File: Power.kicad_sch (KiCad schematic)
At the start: 21 parts, among them IC1 TLV74033PDBVR, J4 USB_C_Receptacle_USB2.0_16P, J9 Conn_01x02, Q1 AO3401A, U3 CH340N, U4 CN3063, U5 TPS7A0522PDBV

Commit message: completed layout and routing with preliminary matching network
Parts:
- renumbered C19 to C20, C27 to C21, C20 to C22, C28 to C23, C30 to C24, C21 to C25, J4 to J2, J9 to J3, R7 to R5, R8 to R6, R5 to R7, R6 to R8, U4 to U3, IC1 to U4, U3 to U5, U5 to U6
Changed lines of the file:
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@@
 		(dnp no)
 		(fields_autoplaced yes)
-		(property "Reference" "#PWR017"
+		(property "Reference" "#PWR024"
 			(at 156.21 67.31 0)
 			(hide yes)
@@
 			(project "WINLAB-LP-Radio-Sensor-Hub"
 				(path "/0de7ee4a-bb98-4bc6-bb89-3afafc4b94b5/5ad374ff-424f-46b2-9f18-b4cecbd24790"
-					(reference "#PWR017")
+					(reference "#PWR024")
 					(unit 1)
 				)
@@
 		(dnp no)
 		(fields_autoplaced yes)
-		(property "Reference" "R7"
+		(property "Reference" "R5"
 			(at 78.74 121.9199 0)
 			(show_name no)
@@
 			(project "WINLAB-LP-Radio-Sensor-Hub"
 				(path "/0de7ee4a-bb98-4bc6-bb89-3afafc4b94b5/5ad374ff-424f-46b2-9f18-b4cecbd24790"
-					(reference "R7")
+					(reference "R5")
 					(unit 1)
 				)
@@
 		(dnp no)
 		(fields_autoplaced yes)
-		(property "Reference" "C20"
+		(property "Reference" "C22"
 			(at 153.67 78.7399 0)
 			(show_name no)
@@
 			(project "WINLAB-LP-Radio-Sensor-Hub"
 				(path "/0de7ee4a-bb98-4bc6-bb89-3afafc4b94b5/5ad374ff-424f-46b2-9f18-b4cecbd24790"
-					(reference "C20")
+					(reference "C22")
 					(unit 1)
 				)
@@
 		(dnp no)
 		(fields_autoplaced yes)
-		(property "Reference" "#PWR029"
+		(property "Reference" "#PWR019"
 			(at 68.58 115.57 0)
 			(hide yes)
@@
 			(project "WINLAB-LP-Radio-Sensor-Hub"
 				(path "/0de7ee4a-bb98-4bc6-bb89-3afafc4b94b5/5ad374ff-424f-46b2-9f18-b4cecbd24790"
-					(reference "#PWR029")
+					(reference "#PWR019")
 					(unit 1)
 				)
@@
 		(dnp no)
 		(fields_autoplaced yes)
-		(property "Reference" "C28"
+		(property "Reference" "C23"
 			(at 173.99 118.1099 0)
 			(show_name no)
@@
 			(project "WINLAB-LP-Radio-Sensor-Hub"
 				(path "/0de7ee4a-bb98-4bc6-bb89-3afafc4b94b5/5ad374ff-424f-46b2-9f18-b4cecbd24790"
-					(reference "C28")
+					(reference "C23")
 					(unit 1)
 				)
@@
 		(dnp no)
 		(fields_autoplaced yes)
-		(property "Reference" "IC1"
+		(property "Reference" "U4"
 			(at 153.67 105.41 0)
 			(show_name no)
@@
 			(project "WINLAB-LP-Radio-Sensor-Hub"
 				(path "/0de7ee4a-bb98-4bc6-bb89-3afafc4b94b5/5ad374ff-424f-46b2-9f18-b4cecbd24790"
-					(reference "IC1")
+					(reference "U4")
 					(unit 1)
 				)
@@
 		(dnp no)
 		(fields_autoplaced yes)
-		(property "Reference" "#PWR015"
+		(property "Reference" "#PWR021"
 			(at 92.71 67.31 0)
 			(hide yes)
@@
 			(project "WINLAB-LP-Radio-Sensor-Hub"
 				(path "/0de7ee4a-bb98-4bc6-bb89-3afafc4b94b5/5ad374ff-424f-46b2-9f18-b4cecbd24790"
-					(reference "#PWR015")
+					(reference "#PWR021")
 					(unit 1)
 				)
@@
 		(dnp no)
 		(fields_autoplaced yes)
-		(property "Reference" "U3"
+		(property "Reference" "U5"
 			(at 206.6133 121.92 0)
 			(show_name no)
@@
 			(project "WINLAB-LP-Radio-Sensor-Hub"
 				(path "/0de7ee4a-bb98-4bc6-bb89-3afafc4b94b5/5ad374ff-424f-46b2-9f18-b4cecbd24790"
-					(reference "U3")
+					(reference "U5")
 					(unit 1)
 				)
@@
 		(dnp no)
 		(fields_autoplaced yes)
-		(property "Reference" "C27"
+		(property "Reference" "C21"
 			(at 129.54 115.5699 0)
 			(show_name no)
@@
 			(project "WINLAB-LP-Radio-Sensor-Hub"
 				(path "/0de7ee4a-bb98-4bc6-bb89-3afafc4b94b5/5ad374ff-424f-46b2-9f18-b4cecbd24790"
-					(reference "C27")
+					(reference "C21")
 					(unit 1)
 				)
@@
 		(dnp no)
 		(fields_autoplaced yes)
-		(property "Reference" "C30"
+		(property "Reference" "C24"
 			(at 217.17 78.7399 0)
 			(show_name no)
@@
 			(project "WINLAB-LP-Radio-Sensor-Hub"
 				(path "/0de7ee4a-bb98-4bc6-bb89-3afafc4b94b5/5ad374ff-424f-46b2-9f18-b4cecbd24790"
-					(reference "C30")
+					(reference "C24")
 					(unit 1)
 				)
@@
 		(dnp no)
 		(fields_autoplaced yes)
-		(property "Reference" "C19"
+		(property "Reference" "C20"
 			(at 101.6 77.4699 0)
 			(show_name no)
@@
 			(project "WINLAB-LP-Radio-Sensor-Hub"
 				(path "/0de7ee4a-bb98-4bc6-bb89-3afafc4b94b5/5ad374ff-424f-46b2-9f18-b4cecbd24790"
-					(reference "C19")
+					(reference "C20")
 					(unit 1)
 				)
@@
 		(dnp no)
 		(fields_autoplaced yes)
-		(property "Reference" "R5"
+		(property "Reference" "R7"
 			(at 139.7 82.5499 0)
 			(show_name no)
@@
 			(project "WINLAB-LP-Radio-Sensor-Hub"
 				(path "/0de7ee4a-bb98-4bc6-bb89-3afafc4b94b5/5ad374ff-424f-46b2-9f18-b4cecbd24790"
-					(reference "R5")
+					(reference "R7")
 					(unit 1)
 				)
@@
 		(dnp no)
 		(fields_autoplaced yes)
-		(property "Reference" "#PWR018"
+		(property "Reference" "#PWR028"
 			(at 262.89 67.31 0)
 			(hide yes)
@@
 			(project "WINLAB-LP-Radio-Sensor-Hub"
 				(path "/0de7ee4a-bb98-4bc6-bb89-3afafc4b94b5/5ad374ff-424f-46b2-9f18-b4cecbd24790"
-					(reference "#PWR018")
+					(reference "#PWR028")
 					(unit 1)
 				)
@@
 		(dnp no)
 		(fields_autoplaced yes)
-		(property "Reference" "#PWR030"
+		(property "Reference" "#PWR023"
 			(at 125.73 116.84 0)
 			(hide yes)
@@
 			(project "WINLAB-LP-Radio-Sensor-Hub"
 				(path "/0de7ee4a-bb98-4bc6-bb89-3afafc4b94b5/5ad374ff-424f-46b2-9f18-b4cecbd24790"
-					(reference "#PWR030")
+					(reference "#PWR023")
 					(unit 1)
 				)
@@
 		(dnp no)
 		(fields_autoplaced yes)
-		(property "Reference" "#PWR028"
+		(property "Reference" "#PWR020"
 			(at 87.63 156.21 0)
 			(hide yes)
@@
 			(project "WINLAB-LP-Radio-Sensor-Hub"
 				(path "/0de7ee4a-bb98-4bc6-bb89-3afafc4b94b5/5ad374ff-424f-46b2-9f18-b4cecbd24790"
-					(reference "#PWR028")
+					(reference "#PWR020")
 					(unit 1)
 				)
@@
 		(dnp no)
 		(fields_autoplaced yes)
-		(property "Reference" "J9"
+		(property "Reference" "J3"
 			(at 180.34 97.7899 90)
 			(show_name no)
@@
 			(project "WINLAB-LP-Radio-Sensor-Hub"
 				(path "/0de7ee4a-bb98-4bc6-bb89-3afafc4b94b5/5ad374ff-424f-46b2-9f18-b4cecbd24790"
-					(reference "J9")
+					(reference "J3")
 					(unit 1)
 				)
@@
 		(dnp no)
 		(fields_autoplaced yes)
-		(property "Reference" "R6"
+		(property "Reference" "R8"
 			(at 196.85 74.9299 0)
 			(show_name no)
@@
 			(project "WINLAB-LP-Radio-Sensor-Hub"
 				(path "/0de7ee4a-bb98-4bc6-bb89-3afafc4b94b5/5ad374ff-424f-46b2-9f18-b4cecbd24790"
-					(reference "R6")
+					(reference "R8")
 					(unit 1)
 				)
@@
 		(dnp no)
 		(fields_autoplaced yes)
-		(property "Reference" "R8"
+		(property "Reference" "R6"
 			(at 90.17 119.3799 0)
 			(show_name no)
@@
 			(project "WINLAB-LP-Radio-Sensor-Hub"
 				(path "/0de7ee4a-bb98-4bc6-bb89-3afafc4b94b5/5ad374ff-424f-46b2-9f18-b4cecbd24790"
-					(reference "R8")
+					(reference "R6")
 					(unit 1)
 				)
@@
 		(dnp no)
 		(fields_autoplaced yes)
-		(property "Reference" "J4"
+		(property "Reference" "J2"
 			(at 45.72 104.14 0)
 			(show_name no)
@@
 			(project "WINLAB-LP-Radio-Sensor-Hub"
 				(path "/0de7ee4a-bb98-4bc6-bb89-3afafc4b94b5/5ad374ff-424f-46b2-9f18-b4cecbd24790"
-					(reference "J4")
+					(reference "J2")
 					(unit 1)
 				)
@@
 		(dnp no)
 		(fields_autoplaced yes)
-		(property "Reference" "U5"
+		(property "Reference" "U6"
 			(at 236.22 63.5 0)
 			(show_name no)
@@
 			(project "WINLAB-LP-Radio-Sensor-Hub"
 				(path "/0de7ee4a-bb98-4bc6-bb89-3afafc4b94b5/5ad374ff-424f-46b2-9f18-b4cecbd24790"
-					(reference "U5")
+					(reference "U6")
 					(unit 1)
 				)
@@
 		(dnp no)
 		(fields_autoplaced yes)
-		(property "Reference" "C21"
+		(property "Reference" "C25"
 			(at 266.7 78.7399 0)
 			(show_name no)
@@
 			(project "WINLAB-LP-Radio-Sensor-Hub"
 				(path "/0de7ee4a-bb98-4bc6-bb89-3afafc4b94b5/5ad374ff-424f-46b2-9f18-b4cecbd24790"
-					(reference "C21")
+					(reference "C25")
 					(unit 1)
 				)
@@
 		(dnp no)
 		(fields_autoplaced yes)
-		(property "Reference" "#PWR016"
+		(property "Reference" "#PWR022"
 			(at 123.19 95.25 0)
 			(hide yes)
@@
 			(project "WINLAB-LP-Radio-Sensor-Hub"
 				(path "/0de7ee4a-bb98-4bc6-bb89-3afafc4b94b5/5ad374ff-424f-46b2-9f18-b4cecbd24790"
-					(reference "#PWR016")
+					(reference "#PWR022")
 					(unit 1)
 				)
@@
 		(dnp no)
 		(fields_autoplaced yes)
-		(property "Reference" "U4"
+		(property "Reference" "U3"
 			(at 123.19 58.42 0)
 			(show_name no)
@@
 			(project "WINLAB-LP-Radio-Sensor-Hub"
 				(path "/0de7ee4a-bb98-4bc6-bb89-3afafc4b94b5/5ad374ff-424f-46b2-9f18-b4cecbd24790"
-					(reference "U4")
-					(unit 1)
-				)
+					(reference "U3")
+					(unit 1)
+				)

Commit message: preliminary JLCPCB BOM, some initial changes for r1
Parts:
- added U8: TPS3839DBZ, Package_TO_SOT_SMD:SOT-23, symbol Power_Supervisor:TPS3839DBZ
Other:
- moved on the sheet: BT1, C20, C22, C24, C25, D2, J3, JP1, Q1, R7, R8, SC1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

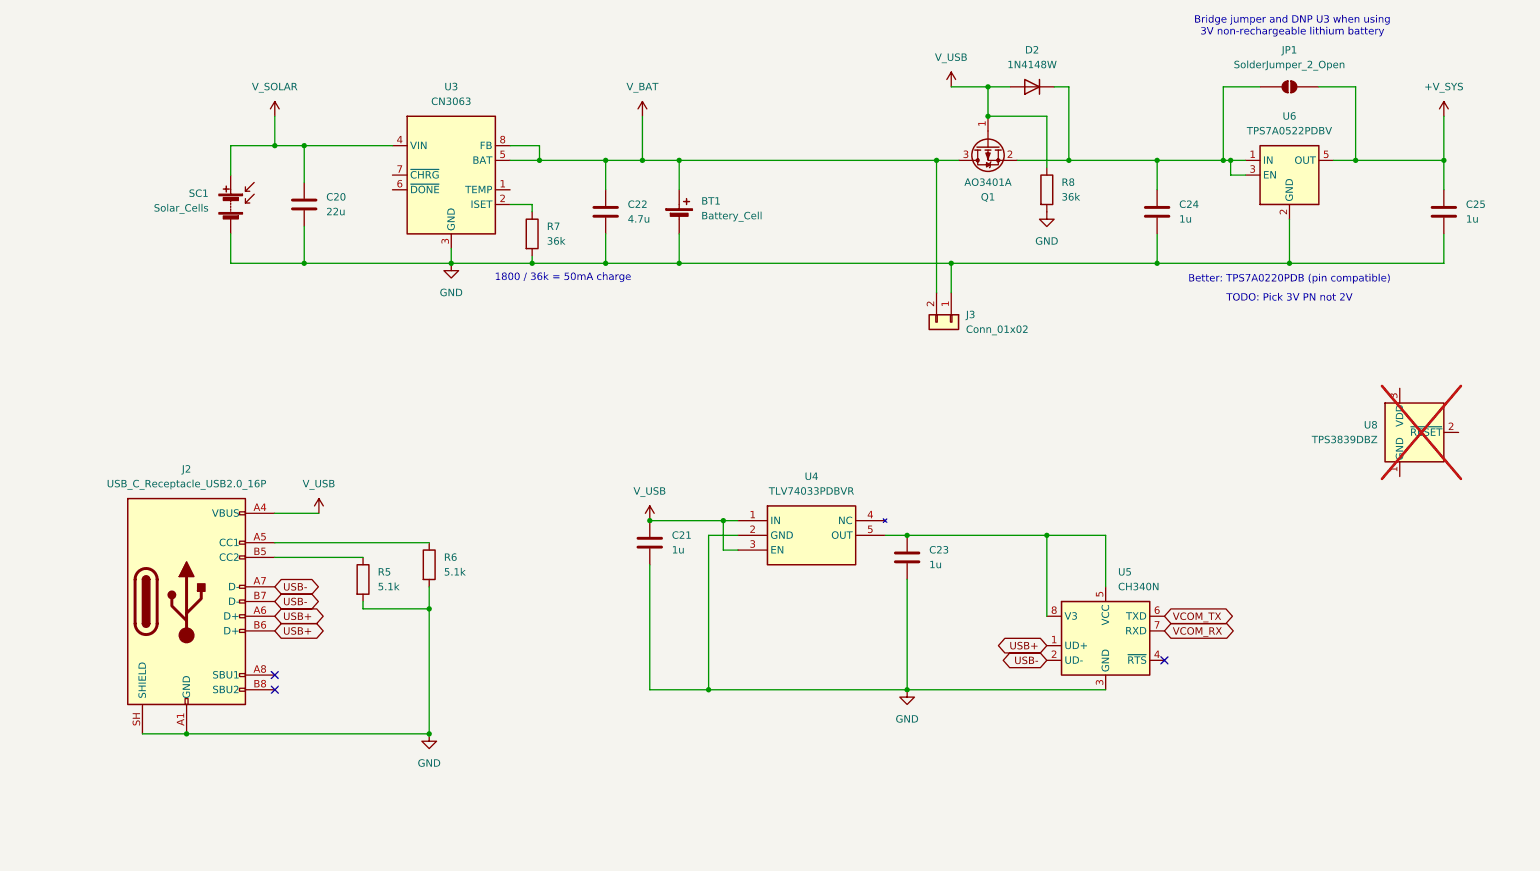
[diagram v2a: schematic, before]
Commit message: USB charging, UVP HW supervisor, PAVDD selection, charger IC enable jumper, layout and silkscreen changes
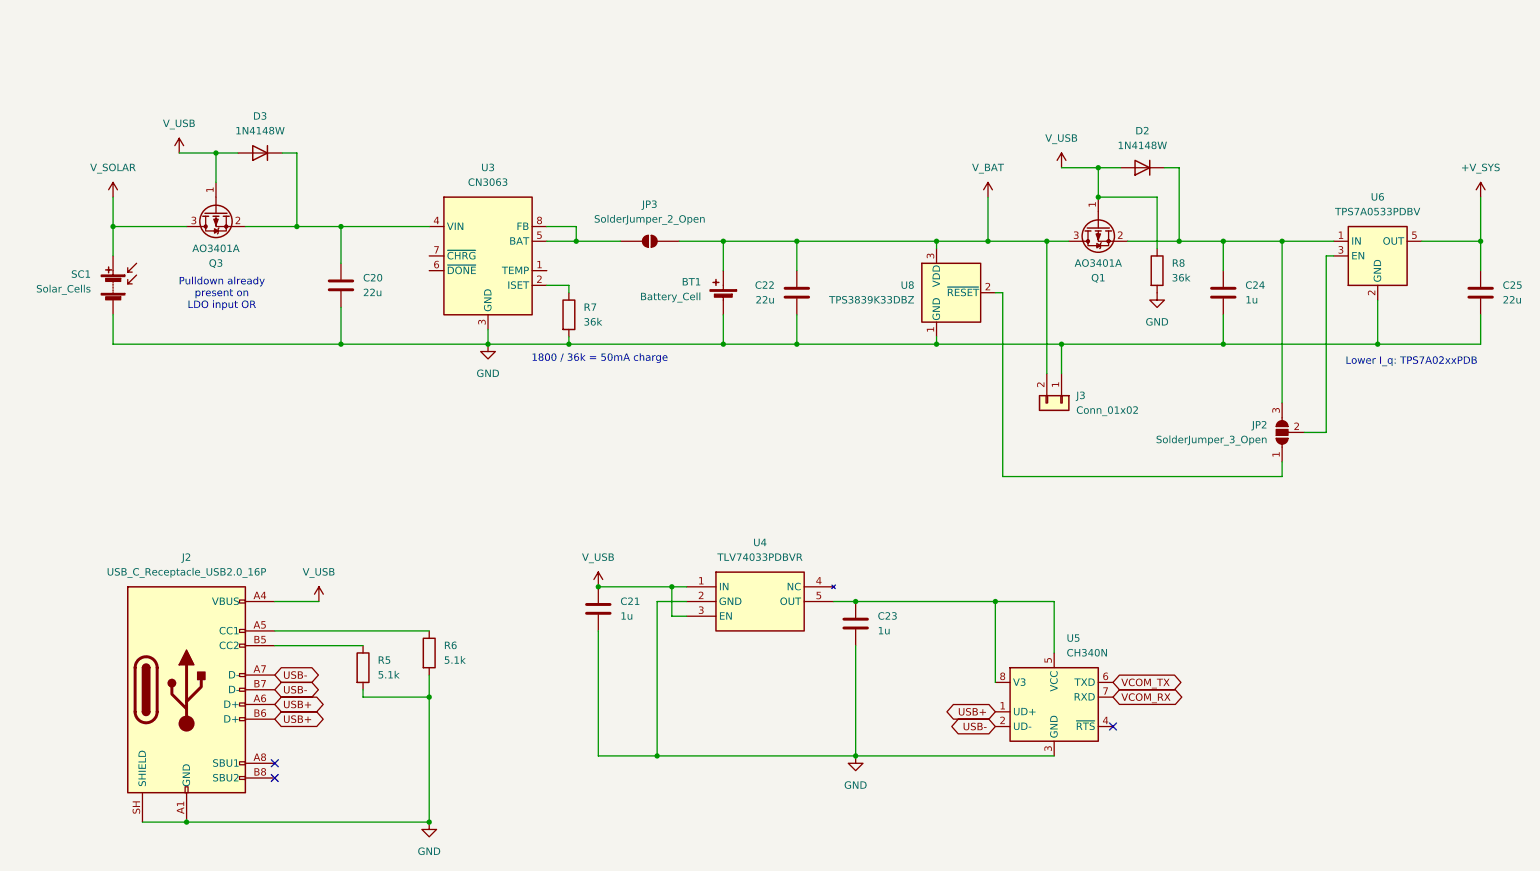
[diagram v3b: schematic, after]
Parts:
- removed JP1: SolderJumper_2_Open, symbol Jumper:SolderJumper_2_Open
- added D3: 1N4148W, Diode_SMD:D_SOD-123, symbol Diode:1N4148W
- added JP2: SolderJumper_3_Open, Jumper:SolderJumper-3_P1.3mm_Open_RoundedPad1.0x1.5mm, symbol Jumper:SolderJumper_3_Open
- added JP3: SolderJumper_2_Open, Jumper:SolderJumper-2_P1.3mm_Open_RoundedPad1.0x1.5mm, symbol Jumper:SolderJumper_2_Open
- added Q3: AO3401A, Package_TO_SOT_SMD:SOT-23, symbol Transistor_FET:AO3401A
- C22: value 4.7u -> 22u
- C25: value 1u -> 22u; footprint Capacitor_SMD:C_0603_1608Metric_Pad1.08x0.95mm_HandSolder -> Capacitor_SMD:C_0805_2012Metric_Pad1.18x1.45mm_HandSolder
- J3: now left out of the parts list
- U6: value TPS7A0522PDBV -> TPS7A0533PDBV
- U8: value TPS3839DBZ -> TPS3839K33DBZ; now fitted
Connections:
- net GND: now also U8.1 (GND)
- net V_BAT: now also U8.3 (VDD), JP3.2 (B); no longer U3.5 (BAT), U3.8 (FB)
- net V_SOLAR: now also Q3.3 (D); no longer C20.1, U3.4 (VIN)
- net V_USB: now also D3.2 (A), Q3.1 (G)
- net at C24.1, D2.1 (K), Q1.2 (S)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: now also JP2.3 (B); no longer U6.3 (EN)
- net at U8.2 (~{RESET}): now also JP2.1 (A)
- new net: C20.1, D3.1 (K), Q3.2 (S), U3.4 (VIN)
- new net: JP2.2 (C), U6.3 (EN)
- new net: JP3.1 (A), U3.5 (BAT), U3.8 (FB)
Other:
- note added: "Lower I_q: TPS7A02xxPDB"
- note added: "Pulldown already present on LDO input OR"
- note removed: "Better: TPS7A0220PDB (pin compatible)"
- note removed: "Bridge jumper and DNP U3 when using 3V non-rechargeable lithium battery"
- note removed: "TODO: Pick 3V PN not 2V"
- moved on the sheet: BT1, C20, C21, C22, C23, C24, D2, J2, J3, Q1, R5, R6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
